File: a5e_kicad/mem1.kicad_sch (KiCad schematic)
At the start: 37 parts, among them U12 IS43LQ32256A-062BLI

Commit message: Add LCSC part numbers and fix C102 footprint
Add a hidden LCSC field to 290 symbols from the JLCPCB parts match
(2026-10-23). Left without LCSC: U7, U15, L1 (not in the JLCPCB
library), C1/C2/C4 and L2-L5 (no value specified), J3 (no confident
match) and Y3 (the 12 pF Basic crystal does not suit the 27 pF load
caps). U2, U12, Y2 and J9 carry the exact-MPN LCSC numbers although
they currently show zero JLCPCB stock.

C102 (22U 6V3) had a 0201 footprint; no 22 uF 0201 part exists. Change
it to 0402 (C415703) like C5-C7.
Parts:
- C44, C47, C48: LCSC (none) -> C415703
- C49, C50, C52, C53, C54, C56, C57, C58, C60, C61, C62, C63, C65, C66, C67, C69, C70, C71, C73, C74, C75, C77, C78, C79, C81, C82, C83, C85, C87, C89, C93: LCSC (none) -> C190183
- R43: LCSC (none) -> C25094
- R44: LCSC (none) -> C11702
- U12: LCSC (none) -> C17416862

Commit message: PCB update: sync with schematic, U12 to SK hynix footprint, J3 annular rings
- Update PCB from schematic: FB1/FB2 PHY ferrite beads, C102 0402,
  R247 to GND, LCSC fields.
- U12 LPDDR4 moves to the SK hynix H9HCNNN8KUMLHR-NME (JLC stock, shared
  with the Agilex 3 and Ti135 boards): new 10 x 15 mm BGA-200 footprint
  in agilex_lib, schematic footprint fields updated.
- Routing and LPDDR4 fixes from the GUI.
- J3 pads 2-38 0.8 -> 0.9 mm (drill 0.6) for JLCPCB's 0.15 mm PTH
  annular ring; 1.0 mm would violate clearance to the tracks between
  the pads.
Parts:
- U12: footprint Package_BGA:BGA-200_10x14.5mm_Layout12x22_P0.8x0.65mm -> agilex_lib:BGA-200_10x15mm_Layout12x22_P0.8x0.65mm
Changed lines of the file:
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@@
 			)
 		)
-		(property "Footprint" "Package_BGA:BGA-200_10x14.5mm_Layout12x22_P0.8x0.65mm"
+		(property "Footprint" "agilex_lib:BGA-200_10x15mm_Layout12x22_P0.8x0.65mm"
 			(at 82.55 200.66 0)
 			(hide yes)
@@
 			)
 		)
-		(property "Footprint" "Package_BGA:BGA-200_10x14.5mm_Layout12x22_P0.8x0.65mm"
+		(property "Footprint" "agilex_lib:BGA-200_10x15mm_Layout12x22_P0.8x0.65mm"
 			(at 82.55 111.76 0)
 			(hide yes)

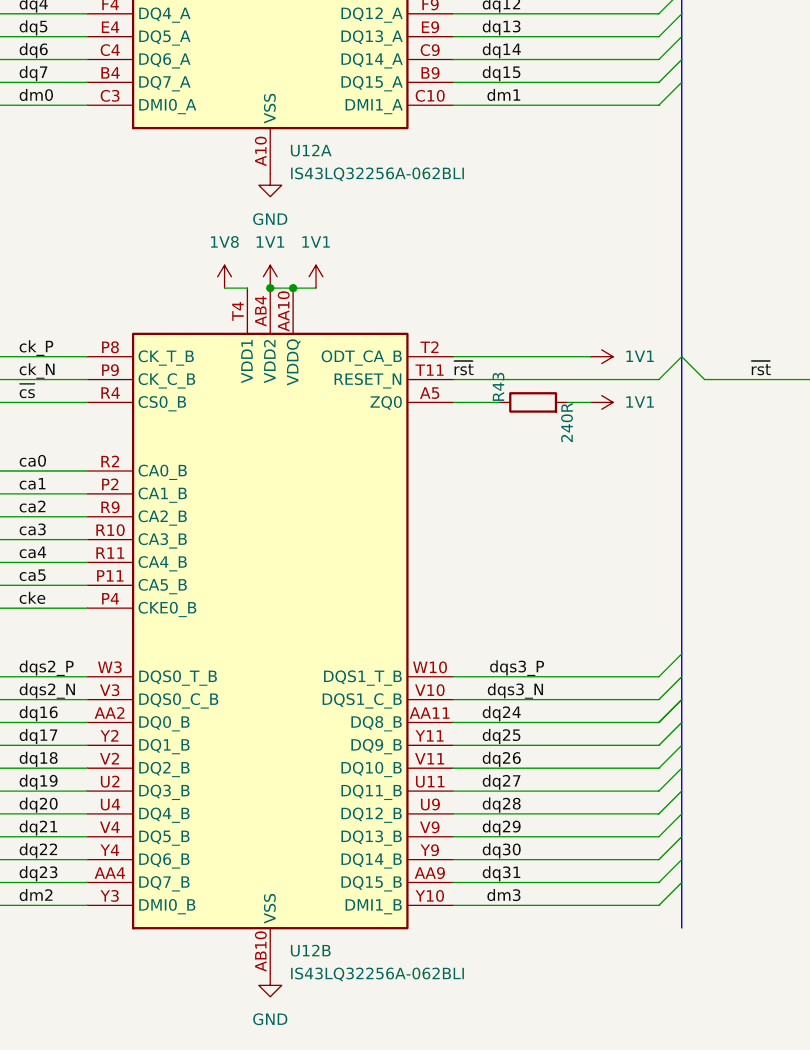
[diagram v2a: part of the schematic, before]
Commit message: U12 -> H9HCNNN8KUMLHR-NME, U2 -> IS25WP128-RHLE (values, LCSC, datasheets)
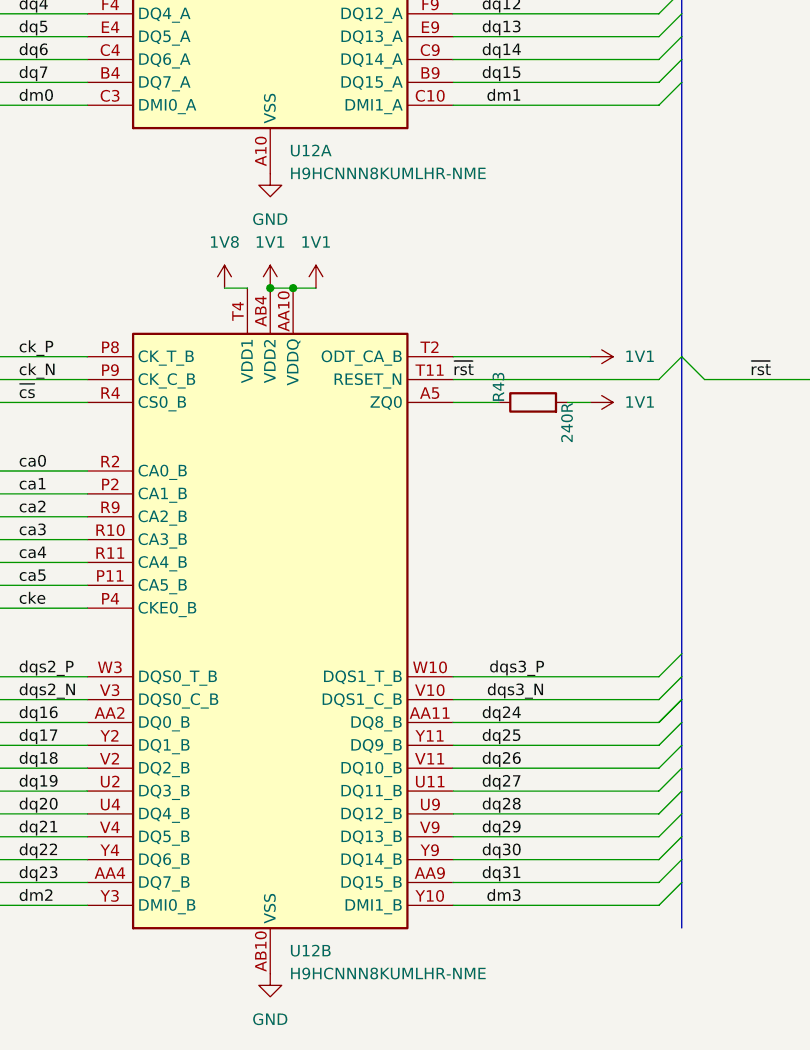
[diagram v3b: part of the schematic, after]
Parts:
- U12: value IS43LQ32256A-062BLI -> H9HCNNN8KUMLHR-NME; LCSC C17416862 -> C2912103
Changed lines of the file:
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@@
 			)
 		)
-		(property "Value" "IS43LQ32256A-062BLI"
+		(property "Value" "H9HCNNN8KUMLHR-NME"
 			(at 83.4233 190.5 0)
 			(show_name no)
@@
 			)
 		)
-		(property "LCSC" "C17416862"
+		(property "LCSC" "C2912103"
 			(at 82.55 200.66 0)
 			(hide yes)
@@
 			)
 		)
-		(property "Datasheet" "http://www.issi.com/WW/pdf/43-46LQ32256A-AL.pdf"
+		(property "Datasheet" "https://www.lcsc.com/datasheet/C2912103.pdf"
 			(at 78.74 182.88 0)
 			(hide yes)
@@
 			)
 		)
-		(property "Description" "256Mx32 bit Low Power Double Data Rate 4 (LPDDR4) SDRAM, 1600 MHz, Industrial, BGA-200"
+		(property "Description" "8Gb LPDDR4 SDRAM, 2 channels x16, 1 CS, 3733 Mbps, 1.8/1.1/1.1 V, FBGA-200 10x15 mm"
 			(at 81.28 152.4 0)
 			(hide yes)
@@
 			)
 		)
-		(property "Value" "IS43LQ32256A-062BLI"
+		(property "Value" "H9HCNNN8KUMLHR-NME"
 			(at 83.4233 101.6 0)
 			(show_name no)
@@
 			)
 		)
-		(property "LCSC" "C17416862"
+		(property "LCSC" "C2912103"
 			(at 82.55 111.76 0)
 			(hide yes)
@@
 			)
 		)
-		(property "Datasheet" "http://www.issi.com/WW/pdf/43-46LQ32256A-AL.pdf"
+		(property "Datasheet" "https://www.lcsc.com/datasheet/C2912103.pdf"
 			(at 78.74 93.98 0)
 			(hide yes)
@@
 			)
 		)
-		(property "Description" "256Mx32 bit Low Power Double Data Rate 4 (LPDDR4) SDRAM, 1600 MHz, Industrial, BGA-200"
+		(property "Description" "8Gb LPDDR4 SDRAM, 2 channels x16, 1 CS, 3733 Mbps, 1.8/1.1/1.1 V, FBGA-200 10x15 mm"
 			(at 81.28 63.5 0)
 			(hide yes)

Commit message: LPDDR4: add 4x 1u (C262-C265) on U12 VDD2/VDDQ 1V1
Mid-frequency decoupling between the 100n under the balls and the 22u bulk.
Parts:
- added C262, C263, C264, C265: 1u, Capacitor_SMD:C_0201_0603Metric, symbol Device:C
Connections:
- net 1V1: now also C262.1, C263.1, C264.1, C265.1
- net GND: now also C262.2, C263.2, C264.2, C265.2

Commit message: C262-C265: 0402 footprint to match the 1u part (C52923)
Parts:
- C262, C263, C264, C265: footprint Capacitor_SMD:C_0201_0603Metric -> Capacitor_SMD:C_0402_1005Metric
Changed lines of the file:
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@@
 			)
 		)
-		(property "Footprint" "Capacitor_SMD:C_0201_0603Metric"
+		(property "Footprint" "Capacitor_SMD:C_0402_1005Metric"
 			(at 178.765 55.88 0)
 			(hide yes)
@@
 			)
 		)
-		(property "Footprint" "Capacitor_SMD:C_0201_0603Metric"
+		(property "Footprint" "Capacitor_SMD:C_0402_1005Metric"
 			(at 186.385 55.88 0)
 			(hide yes)
@@
 			)
 		)
-		(property "Footprint" "Capacitor_SMD:C_0201_0603Metric"
+		(property "Footprint" "Capacitor_SMD:C_0402_1005Metric"
 			(at 194.005 55.88 0)
 			(hide yes)
@@
 			)
 		)
-		(property "Footprint" "Capacitor_SMD:C_0201_0603Metric"
+		(property "Footprint" "Capacitor_SMD:C_0402_1005Metric"
 			(at 201.625 55.88 0)
 			(hide yes)

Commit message: Schematic reorg step 1: remove dangling stubs and stale notes, correct notes, fill title blocks
Netlist: 0 renamed, 0 connectivity diffs; DRC parity 0. ERC 315 -> 242.
Plan refreshed for the eMMC, RTL8211FDI, TPS548A28 and the tuned LPDDR4 (IOBANK 3 sheet name kept).
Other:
- title: (none) -> LPDDR4 memory and decoupling
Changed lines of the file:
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@@
 	(paper "A4")
 	(title_block
-		(rev "0.1")
+		(title "LPDDR4 memory and decoupling")
+		(rev "${REVISION}")
+		(comment 1 "${BOARD}")
 	)
 	(junction

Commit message: Schematic reorg step 2: per-rail power symbols, real GND symbols, PWR_FLAGs, U12 in project library
Netlist: 0 renamed, 0 connectivity diffs; DRC parity 0. ERC 234 -> 224 (with the KiCad symbol libraries).
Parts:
- U12: symbol Memory_RAM:IS43LQ32256A-062BLI -> agilex_5_lib:IS43LQ32256A-062BLI
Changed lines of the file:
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@@
 	)
 	(symbol
-		(lib_id "power:+1V1")
+		(lib_id "agilex_5_lib:1V1")
 		(at 81.28 114.3 0)
 		(unit 1)
@@
 	)
 	(symbol
-		(lib_id "power:+1V1")
+		(lib_id "agilex_5_lib:1V1")
 		(at 154.94 35.56 90)
 		(mirror x)
@@
 	)
 	(symbol
-		(lib_id "power:+1V1")
+		(lib_id "agilex_5_lib:1V8")
 		(at 154.94 62.23 90)
 		(mirror x)
@@
 	)
 	(symbol
-		(lib_id "power:+1V1")
-		(at 152.4 124.46 270)
+		(lib_id "power:GND")
+		(at 152.4 124.46 90)
 		(unit 1)
 		(body_style 1)
@@
 	)
 	(symbol
-		(lib_id "power:+1V1")
-		(at 154.94 43.18 90)
+		(lib_id "power:GND")
+		(at 154.94 43.18 270)
 		(mirror x)
 		(unit 1)
@@
 	)
 	(symbol
-		(lib_id "power:+1V1")
+		(lib_id "agilex_5_lib:1V1")
 		(at 154.94 22.86 90)
 		(mirror x)
@@
 	)
 	(symbol
-		(lib_id "power:+1V1")
+		(lib_id "agilex_5_lib:1V8")
 		(at 76.2 25.4 0)
 		(unit 1)
@@
 	)
 	(symbol
-		(lib_id "power:+1V1")
+		(lib_id "agilex_5_lib:1V1")
 		(at 116.84 33.02 270)
 		(unit 1)
@@
 	)
 	(symbol
-		(lib_id "power:+1V1")
+		(lib_id "agilex_5_lib:1V1")
 		(at 116.84 121.92 270)
 		(unit 1)
@@
 	)
 	(symbol
-		(lib_id "power:+1V1")
+		(lib_id "agilex_5_lib:1V1")
 		(at 154.94 48.26 90)
 		(mirror x)
@@
 	)
 	(symbol
-		(lib_id "power:+1V1")
+		(lib_id "agilex_5_lib:1V1")
 		(at 86.36 114.3 0)
 		(unit 1)
@@
 	)
 	(symbol
-		(lib_id "power:+1V1")
-		(at 154.94 30.48 90)
+		(lib_id "power:GND")
+		(at 154.94 30.48 270)
 		(mirror x)
 		(unit 1)
@@
 	)
 	(symbol
-		(lib_id "Memory_RAM:IS43LQ32256A-062BLI")
+		(lib_id "agilex_5_lib:IS43LQ32256A-062BLI")
 		(at 81.28 152.4 0)
 		(unit 2)
@@
 	)
 	(symbol
-		(lib_id "power:+1V1")
-		(at 154.94 55.88 90)
+		(lib_id "power:GND")
+		(at 154.94 55.88 270)
 		(mirror x)
 		(unit 1)
@@
 	)
 	(symbol
-		(lib_id "power:+1V1")
+		(lib_id "agilex_5_lib:1V1")
 		(at 86.36 25.4 0)
 		(unit 1)
@@
 	)
 	(symbol
-		(lib_id "power:+1V1")
-		(at 154.94 69.85 90)
+		(lib_id "power:GND")
+		(at 154.94 69.85 270)
 		(mirror x)
 		(unit 1)
@@
 	)
 	(symbol
-		(lib_id "power:+1V1")
+		(lib_id "agilex_5_lib:1V1")
 		(at 116.84 127 270)
 		(unit 1)
@@
 	)
 	(symbol
-		(lib_id "Memory_RAM:IS43LQ32256A-062BLI")
+		(lib_id "agilex_5_lib:IS43LQ32256A-062BLI")
 		(at 81.28 63.5 0)
 		(unit 1)
@@
 	)
 	(symbol
-		(lib_id "power:+1V1")
+		(lib_id "agilex_5_lib:1V8")
 		(at 76.2 114.3 0)
 		(unit 1)
@@
 	)
 	(symbol
-		(lib_id "power:+1V1")
+		(lib_id "agilex_5_lib:1V1")
 		(at 81.28 25.4 0)
 		(unit 1)
